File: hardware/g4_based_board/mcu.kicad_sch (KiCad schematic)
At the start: 17 parts, among them SW2 RESET, SW9 SW_SPDT, U7 STM32G431R6Tx, Y1 12MHz, 20pF

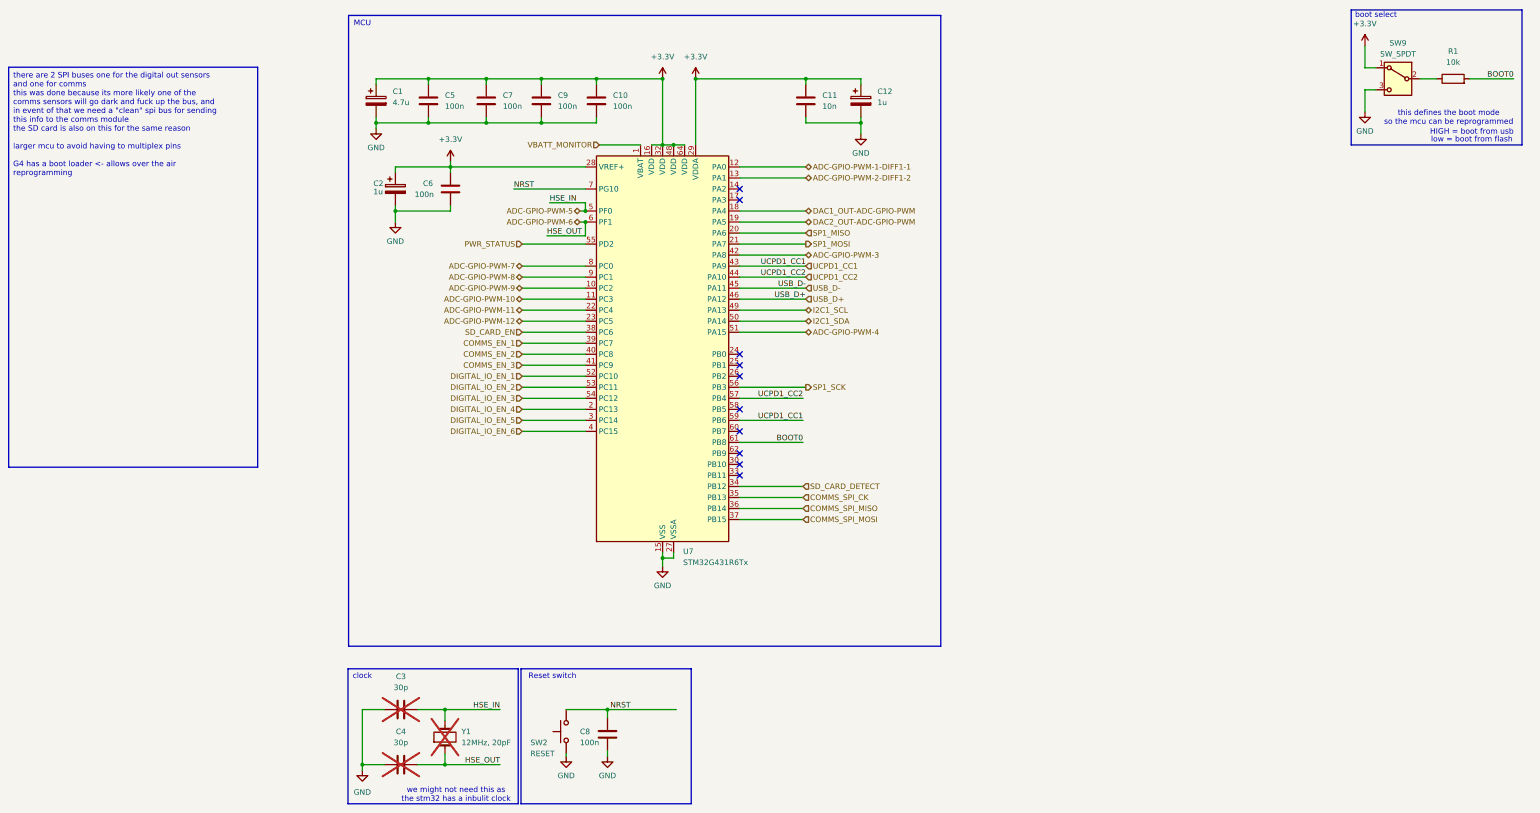
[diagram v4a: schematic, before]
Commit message: replaced orignal switch to avoid ERC error
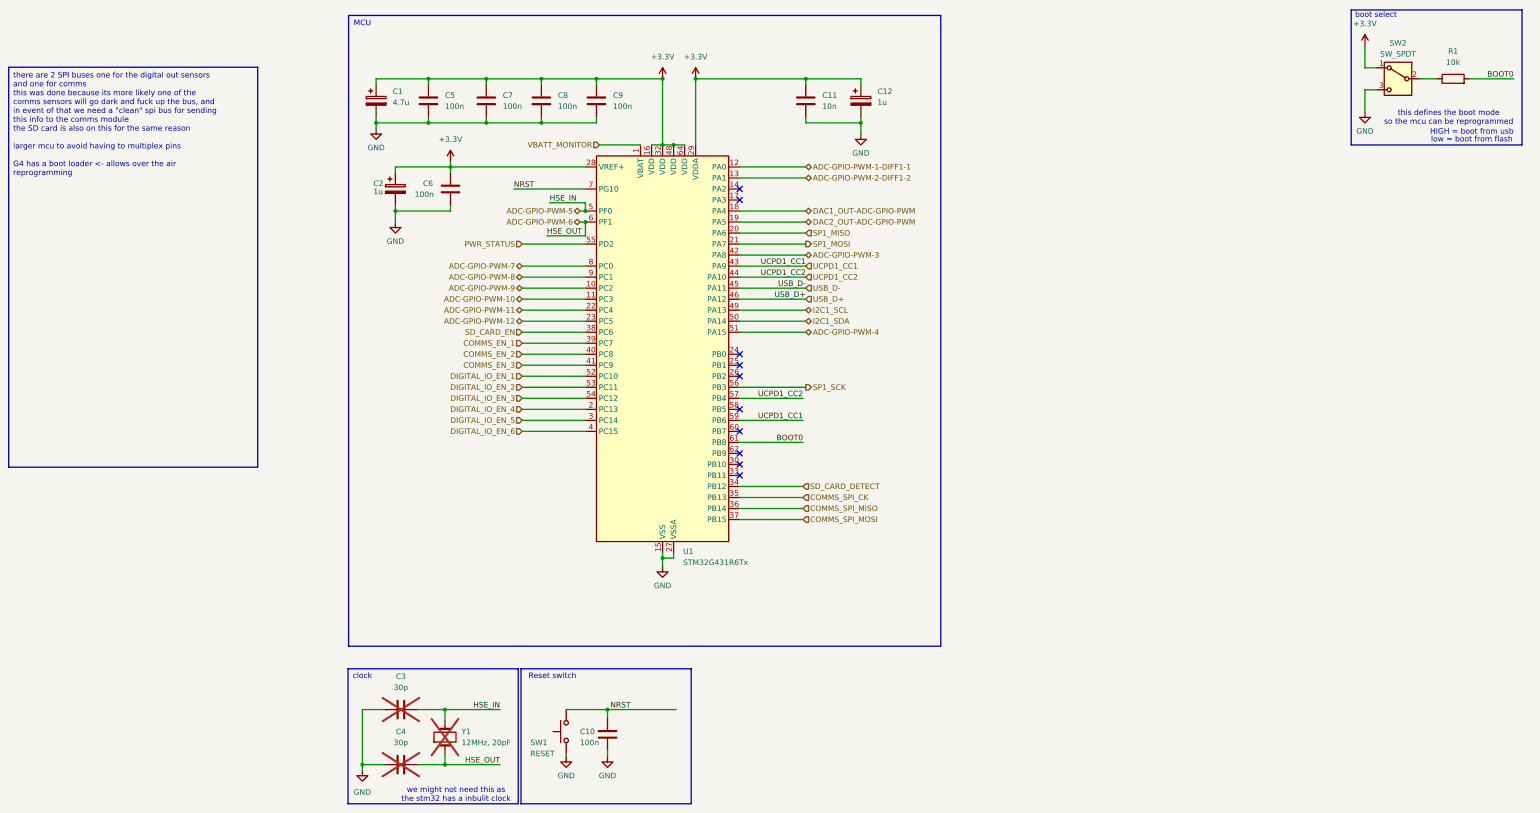
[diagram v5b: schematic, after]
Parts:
- renumbered C8 to C10, C9 to C8, C10 to C9, SW2 to SW1, SW9 to SW2, U7 to U1
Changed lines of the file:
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@@
 		(dnp no)
 		(fields_autoplaced yes)
-		(property "Reference" "#PWR02"
+		(property "Reference" "#PWR021"
 			(at 85.725 32.385 0)
 			(effects
@@
 			(project "data_logger"
 				(path "/9bc93932-ff5f-4f35-96cf-dfa5f042acb6/9c8c2a3d-9bd9-4776-9fa4-86dd96b005ae"
-					(reference "#PWR02")
+					(reference "#PWR021")
 					(unit 1)
 				)
@@
 		(on_board yes)
 		(dnp no)
-		(property "Reference" "C8"
+		(property "Reference" "C10"
 			(at 66.675 179.07 0)
 			(effects
@@
 			(project "data_logger"
 				(path "/9bc93932-ff5f-4f35-96cf-dfa5f042acb6/9c8c2a3d-9bd9-4776-9fa4-86dd96b005ae"
-					(reference "C8")
+					(reference "C10")
 					(unit 1)
 				)
@@
 		(dnp no)
 		(fields_autoplaced yes)
-		(property "Reference" "#PWR07"
+		(property "Reference" "#PWR026"
 			(at 247.65 42.545 0)
 			(effects
@@
 			(project "data_logger"
 				(path "/9bc93932-ff5f-4f35-96cf-dfa5f042acb6/9c8c2a3d-9bd9-4776-9fa4-86dd96b005ae"
-					(reference "#PWR07")
+					(reference "#PWR026")
 					(unit 1)
 				)
@@
 		(dnp no)
 		(fields_autoplaced yes)
-		(property "Reference" "#PWR010"
+		(property "Reference" "#PWR022"
 			(at 85.725 147.32 0)
 			(effects
@@
 			(project "data_logger"
 				(path "/9bc93932-ff5f-4f35-96cf-dfa5f042acb6/9c8c2a3d-9bd9-4776-9fa4-86dd96b005ae"
-					(reference "#PWR010")
+					(reference "#PWR022")
 					(unit 1)
 				)
@@
 		(dnp no)
 		(fields_autoplaced yes)
-		(property "Reference" "C9"
+		(property "Reference" "C8"
 			(at 61.595 32.385 0)
 			(effects
@@
 			(project "data_logger"
 				(path "/9bc93932-ff5f-4f35-96cf-dfa5f042acb6/9c8c2a3d-9bd9-4776-9fa4-86dd96b005ae"
-					(reference "C9")
+					(reference "C8")
 					(unit 1)
 				)
@@
 		(dnp no)
 		(fields_autoplaced yes)
-		(property "Reference" "#PWR08"
+		(property "Reference" "#PWR020"
 			(at 73.025 191.135 0)
 			(effects
@@
 			(project "data_logger"
 				(path "/9bc93932-ff5f-4f35-96cf-dfa5f042acb6/9c8c2a3d-9bd9-4776-9fa4-86dd96b005ae"
-					(reference "#PWR08")
+					(reference "#PWR020")
 					(unit 1)
 				)
@@
 		(on_board yes)
 		(dnp no)
-		(property "Reference" "SW9"
+		(property "Reference" "SW2"
 			(at 255.27 20.32 0)
 			(effects
@@
 			(project "data_logger"
 				(path "/9bc93932-ff5f-4f35-96cf-dfa5f042acb6/9c8c2a3d-9bd9-4776-9fa4-86dd96b005ae"
-					(reference "SW9")
+					(reference "SW2")
 					(unit 1)
 				)
@@
 		(dnp no)
 		(fields_autoplaced yes)
-		(property "Reference" "#PWR04"
+		(property "Reference" "#PWR018"
 			(at 36.83 51.435 0)
 			(effects
@@
 			(project "data_logger"
 				(path "/9bc93932-ff5f-4f35-96cf-dfa5f042acb6/9c8c2a3d-9bd9-4776-9fa4-86dd96b005ae"
-					(reference "#PWR04")
+					(reference "#PWR018")
 					(unit 1)
 				)
@@
 		(dnp no)
 		(fields_autoplaced yes)
-		(property "Reference" "#PWR01"
+		(property "Reference" "#PWR017"
 			(at 24.13 67.945 0)
 			(effects
@@
 			(project "data_logger"
 				(path "/9bc93932-ff5f-4f35-96cf-dfa5f042acb6/9c8c2a3d-9bd9-4776-9fa4-86dd96b005ae"
-					(reference "#PWR01")
+					(reference "#PWR017")
 					(unit 1)
 				)
@@
 		(dnp no)
 		(fields_autoplaced yes)
-		(property "Reference" "#PWR09"
+		(property "Reference" "#PWR023"
 			(at 93.345 32.385 0)
 			(effects
@@
 			(project "data_logger"
 				(path "/9bc93932-ff5f-4f35-96cf-dfa5f042acb6/9c8c2a3d-9bd9-4776-9fa4-86dd96b005ae"
-					(reference "#PWR09")
+					(reference "#PWR023")
 					(unit 1)
 				)
@@
 		(dnp no)
 		(fields_autoplaced yes)
-		(property "Reference" "U7"
+		(property "Reference" "U1"
 			(at 90.4591 137.541 0)
 			(effects
@@
 			(project "data_logger"
 				(path "/9bc93932-ff5f-4f35-96cf-dfa5f042acb6/9c8c2a3d-9bd9-4776-9fa4-86dd96b005ae"
-					(reference "U7")
+					(reference "U1")
 					(unit 1)
 				)
@@
 		(dnp no)
 		(fields_autoplaced yes)
-		(property "Reference" "#PWR05"
+		(property "Reference" "#PWR019"
 			(at 63.5 191.135 0)
 			(effects
@@
 			(project "data_logger"
 				(path "/9bc93932-ff5f-4f35-96cf-dfa5f042acb6/9c8c2a3d-9bd9-4776-9fa4-86dd96b005ae"
-					(reference "#PWR05")
+					(reference "#PWR019")
 					(unit 1)
 				)
@@
 		(dnp no)
 		(fields_autoplaced yes)
-		(property "Reference" "#PWR03"
+		(property "Reference" "#PWR015"
 			(at 16.51 194.31 0)
 			(effects
@@
 			(project "data_logger"
 				(path "/9bc93932-ff5f-4f35-96cf-dfa5f042acb6/9c8c2a3d-9bd9-4776-9fa4-86dd96b005ae"
-					(reference "#PWR03")
+					(reference "#PWR015")
 					(unit 1)
 				)
@@
 		(dnp no)
 		(fields_autoplaced yes)
-		(property "Reference" "#PWR011"
+		(property "Reference" "#PWR024"
 			(at 131.445 47.625 0)
 			(effects
@@
 			(project "data_logger"
 				(path "/9bc93932-ff5f-4f35-96cf-dfa5f042acb6/9c8c2a3d-9bd9-4776-9fa4-86dd96b005ae"
-					(reference "#PWR011")
+					(reference "#PWR024")
 					(unit 1)
 				)
@@
 		(dnp no)
 		(fields_autoplaced yes)
-		(property "Reference" "#PWR06"
+		(property "Reference" "#PWR025"
 			(at 247.65 24.765 0)
 			(effects
@@
 			(project "data_logger"
 				(path "/9bc93932-ff5f-4f35-96cf-dfa5f042acb6/9c8c2a3d-9bd9-4776-9fa4-86dd96b005ae"
-					(reference "#PWR06")
+					(reference "#PWR025")
 					(unit 1)
 				)
@@
 		(dnp no)
 		(fields_autoplaced yes)
-		(property "Reference" "C10"
+		(property "Reference" "C9"
 			(at 74.295 32.385 0)
 			(effects
@@
 			(project "data_logger"
 				(path "/9bc93932-ff5f-4f35-96cf-dfa5f042acb6/9c8c2a3d-9bd9-4776-9fa4-86dd96b005ae"
-					(reference "C10")
+					(reference "C9")
 					(unit 1)
 				)
@@
 		(dnp no)
 		(fields_autoplaced yes)
-		(property "Reference" "#PWR039"
+		(property "Reference" "#PWR016"
 			(at 19.685 46.355 0)
 			(effects
@@
 			(project "data_logger"
 				(path "/9bc93932-ff5f-4f35-96cf-dfa5f042acb6/9c8c2a3d-9bd9-4776-9fa4-86dd96b005ae"
-					(reference "#PWR039")
+					(reference "#PWR016")
 					(unit 1)
 				)
@@
 		(on_board yes)
 		(dnp no)
-		(property "Reference" "SW2"
+		(property "Reference" "SW1"
 			(at 55.245 181.61 90)
 			(effects
@@
 			(project "data_logger"
 				(path "/9bc93932-ff5f-4f35-96cf-dfa5f042acb6/9c8c2a3d-9bd9-4776-9fa4-86dd96b005ae"
-					(reference "SW2")
-					(unit 1)
-				)
+					(reference "SW1")
+					(unit 1)
+				)

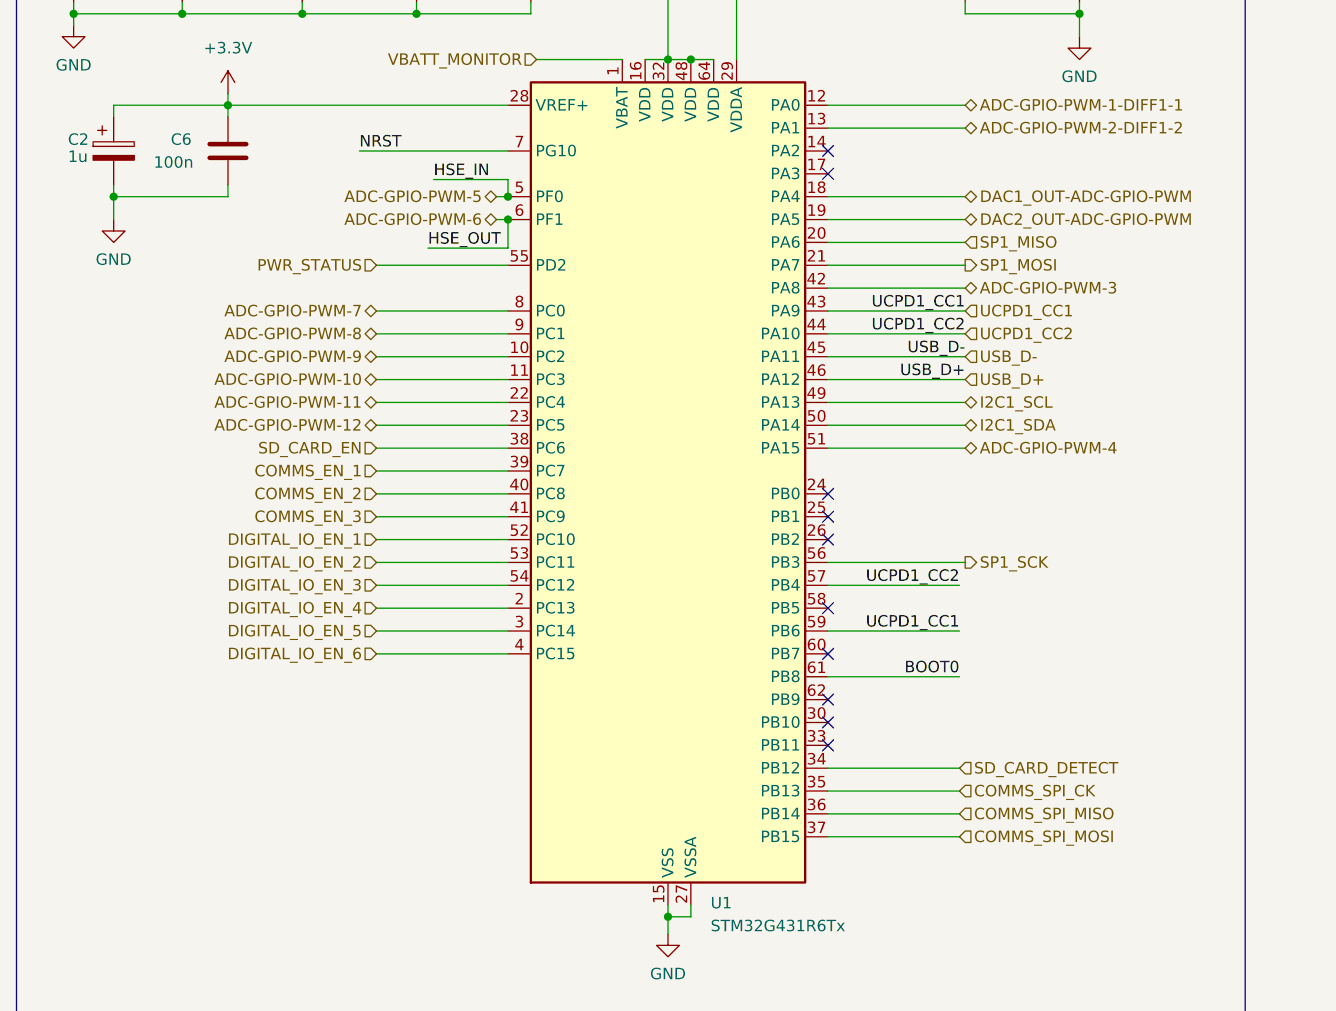
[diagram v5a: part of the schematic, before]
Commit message: added usart, buttons and made sure each pin is allocated correctly
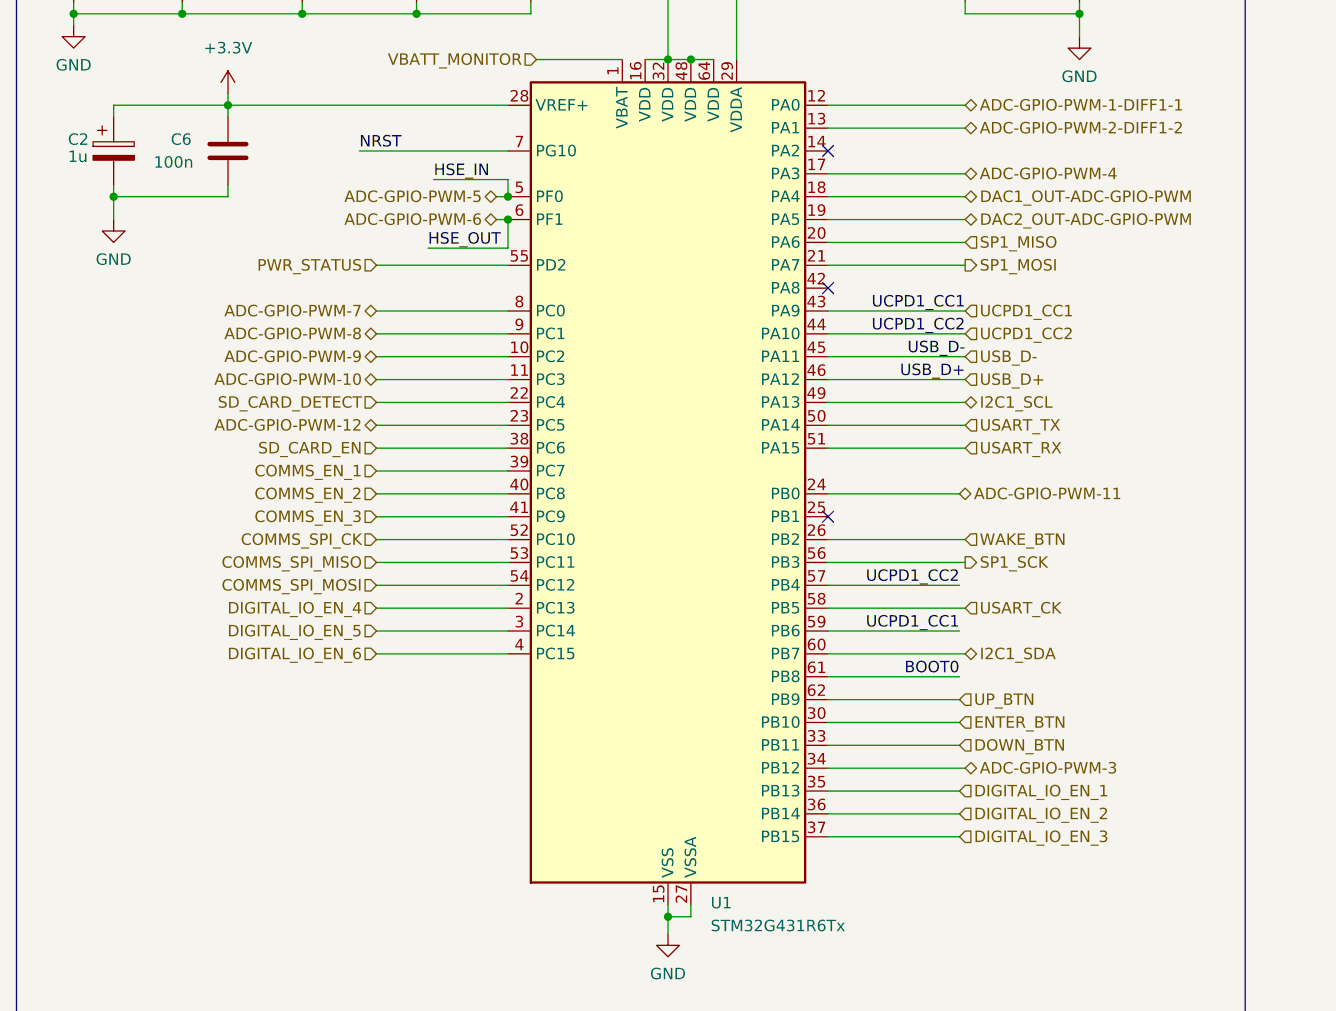
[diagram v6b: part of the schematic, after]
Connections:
- net ADC-GPIO-PWM-11: now also U1.24 (PB0); no longer U1.22 (PC4)
- net ADC-GPIO-PWM-3: now also U1.34 (PB12); no longer U1.42 (PA8)
- net ADC-GPIO-PWM-4: now also U1.17 (PA3); no longer U1.51 (PA15)
- net COMMS_SPI_CK: now also U1.52 (PC10); no longer U1.35 (PB13)
- net COMMS_SPI_MISO: now also U1.53 (PC11); no longer U1.36 (PB14)
- net COMMS_SPI_MOSI: now also U1.54 (PC12); no longer U1.37 (PB15)
- net DIGITAL_IO_EN_1: now also U1.35 (PB13); no longer U1.52 (PC10)
- net DIGITAL_IO_EN_2: now also U1.36 (PB14); no longer U1.53 (PC11)
- net DIGITAL_IO_EN_3: now also U1.37 (PB15); no longer U1.54 (PC12)
- net I2C1_SDA: now also U1.60 (PB7); no longer U1.50 (PA14)
- net SD_CARD_DETECT: now also U1.22 (PC4); no longer U1.34 (PB12)
- net WAKE_BTN: now reaches U1.26 (PB2)
- net ENTER_BTN: now reaches U1.30 (PB10)
- net DOWN_BTN: now reaches U1.33 (PB11)
- net USART_CK: now reaches U1.58 (PB5)
- net UP_BTN: now reaches U1.62 (PB9)
- new net USART_RX: U1.51 (PA15)
- new net USART_TX: U1.50 (PA14)
- no-connect marks 10 -> 3

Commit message: rev-1
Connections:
- net COMMS_EN_1: now also U1.38 (PC6); no longer U1.39 (PC7)
- net COMMS_EN_2: now also U1.39 (PC7); no longer U1.40 (PC8)
- net COMMS_EN_3: now also U1.40 (PC8); no longer U1.41 (PC9)
- net DIGITAL_IO_EN_4: now also U1.25 (PB1); no longer U1.2 (PC13)
- net DIGITAL_IO_EN_5: now also U1.30 (PB10); no longer U1.3 (PC14)
- net DIGITAL_IO_EN_6: now also U1.33 (PB11); no longer U1.4 (PC15)
- net DOWN_BTN: now also U1.2 (PC13); no longer U1.33 (PB11)
- net ENTER_BTN: now also U1.4 (PC15); no longer U1.30 (PB10)
- net PWR_STATUS: now also U1.26 (PB2); no longer U1.55 (PD2)
- net SD_CARD_DETECT: now also U1.62 (PB9); no longer U1.22 (PC4)
- net SD_CARD_EN: now also U1.41 (PC9); no longer U1.38 (PC6)
- net UP_BTN: now also U1.3 (PC14); no longer U1.62 (PB9)
- net WAKE_BTN: now also U1.14 (PA2); no longer U1.26 (PB2)
- no-connect marks 3 -> 1
